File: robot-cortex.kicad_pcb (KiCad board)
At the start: 2 copper layers, 11 parts, among them U3 DF52-5S-0.8H(21)

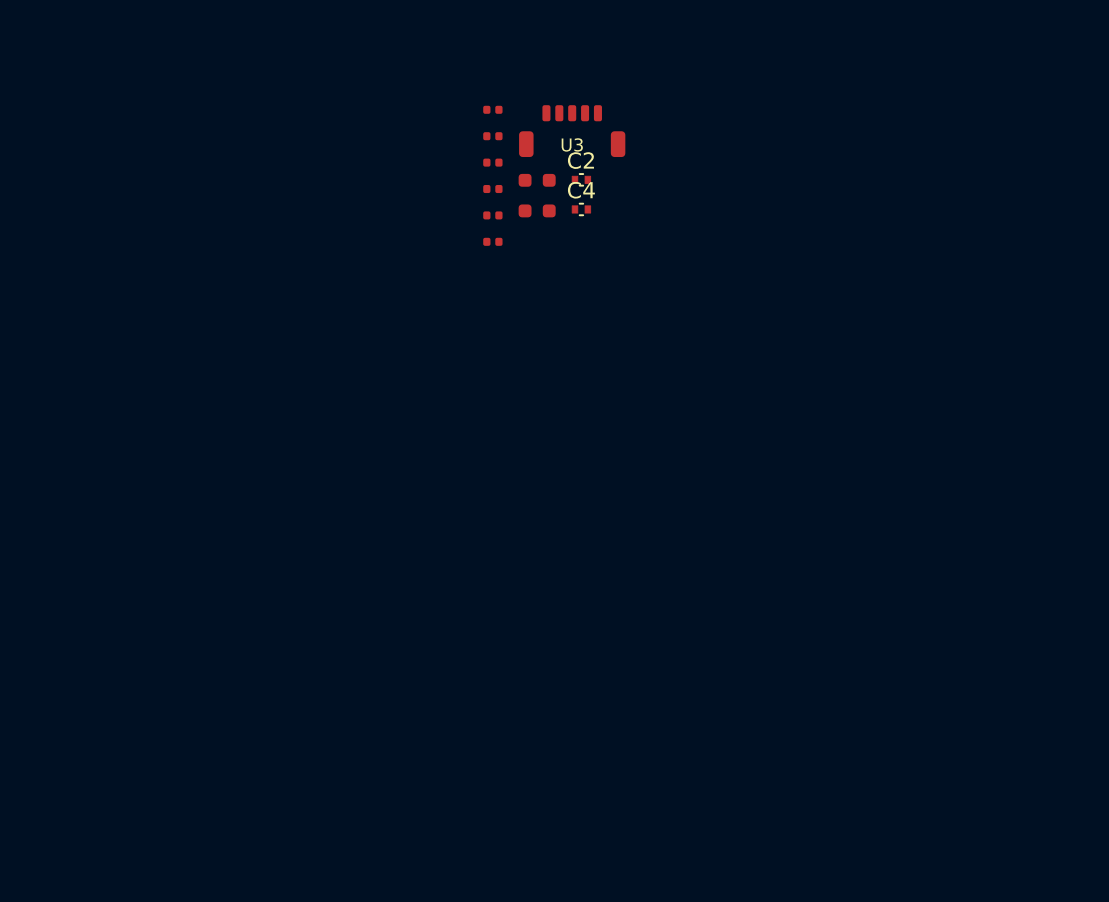
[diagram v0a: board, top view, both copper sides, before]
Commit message: added many components
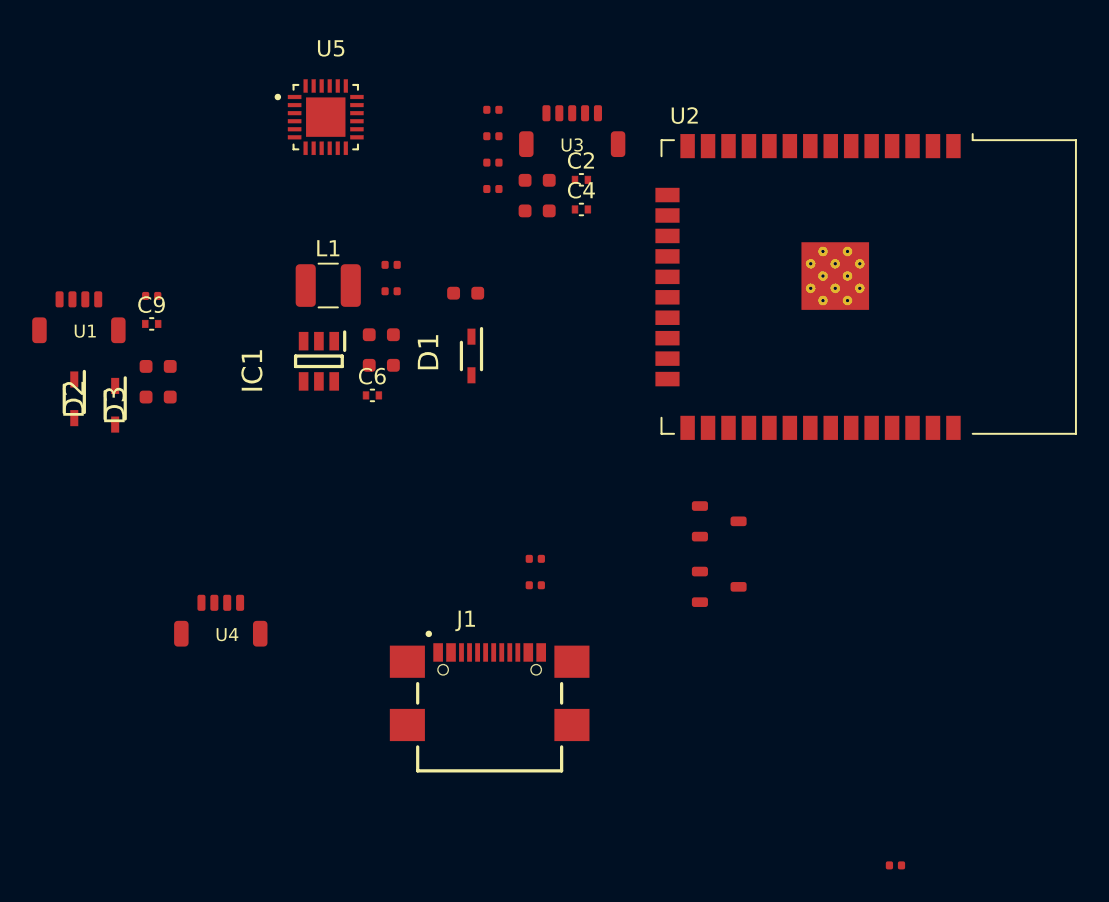
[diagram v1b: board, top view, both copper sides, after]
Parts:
- added C10: 4.7uF, robot-cortex:C_0603_1608Metric, F.Cu at (54.5, 58.2)
- added C11: 4.7uF, robot-cortex:C_0603_1608Metric, F.Cu at (54.5, 60.1)
- added C5: 4.7uF, robot-cortex:C_0603_1608Metric, F.Cu at (73.6, 53.6)
- added C6: 100nF, robot-cortex:C_0402_1005Metric, F.Cu at (67.8, 60.0)
- added C7: 4.7uF, robot-cortex:C_0603_1608Metric, F.Cu at (68.4, 56.2)
- added C8: 4.7uF, robot-cortex:C_0603_1608Metric, F.Cu at (68.4, 58.1)
- added C9: 100nF, robot-cortex:C_0402_1005Metric, F.Cu at (54.1, 55.5)
- added D1: NSR0530HT1G, robot-cortex:SOD2512X110N, F.Cu at (74.0, 57.5)
- added D2: NSR0530HT1G, robot-cortex:SOD2512X110N, F.Cu at (49.3, 60.2)
- added D3: NSR0530HT1G, robot-cortex:SOD2512X110N, F.Cu at (51.9, 60.6)
- added IC1: ADP2301AUJZ-R7, robot-cortex:SOT95P280X100-6N, F.Cu at (64.5, 57.8)
- added J1: USB4110GFA, robot-cortex:GCT_USB4110GFA, F.Cu at (75.1, 77.0)
- added L1: 2.2uH, Inductor_SMD:L_1210_3225Metric, F.Cu at (65.1, 53.1)
- added Q1: NPN, robot-cortex:SOT-23-3, F.Cu at (89.4, 67.8)
- added Q2: NPN, robot-cortex:SOT-23-3, F.Cu at (89.4, 71.8)
- added R11: 10.2k, robot-cortex:R_0402_1005Metric, F.Cu at (69.0, 53.5)
- added R7: 5.1k, robot-cortex:R_0402_1005Metric, F.Cu at (77.9, 70.1)
- added R8: 5.1k, robot-cortex:R_0402_1005Metric, F.Cu at (77.9, 71.8)
- added R9: 1k, robot-cortex:R_0402_1005Metric, F.Cu at (100.3, 89.2)
- added U1: DF52-4S-0.8H(21), robot-cortex:DF52-4S-0.8H(21), F.Cu at (49.6, 54.0)
- added U2: ESP32-WROOM-32E-H4, robot-cortex:ESP32-WROOM-32, F.Cu at (95.7, 53.2)
- added U4: DF52-4S-0.8H(21), robot-cortex:DF52-4S-0.8H(21), F.Cu at (58.4, 72.8)
- added U5: CP2102N-A02-GQFN24R, robot-cortex:QFN50P400X400X80-25N, F.Cu at (64.9, 42.7)
- R5: value 10k -> 31.6k
- R6: value 2k -> 10k
- moved R6 21.5 mm to (54.1, 53.8)
- moved R5 7.03 mm to (69.0, 51.9)
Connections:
- C1 pad 1: /3V3 -> 3v3
- C2 pad 1: /3V3 -> 3v3
- C3 pad 1: /3V3 -> 3v3
- C4 pad 1: /3V3 -> 3v3
- R5 pad 1: Net-(U1-SUSPENDb) -> /3V3-Supply/FB
- R5 pad 2: GND -> 3v3
- R6 pad 1: Net-(U1-RSTb) -> /EN
- R6 pad 2: /3V3 -> 3v3

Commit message: checked and fixed npn issue, added mpn
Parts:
- Q1, Q2: value NPN -> SS8050-G
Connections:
- Q1 pad 2: /EN -> /RTS
- Q1 pad 3: /RTS -> /EN
- Q2 pad 2: /IO0 -> /DTR
- Q2 pad 3: /DTR -> /IO0
- U5 pad 10: (no net) -> unconnected-(U5-NC-Pad10)
- U5 pad 16: (no net) -> unconnected-(U5-NC-Pad16)
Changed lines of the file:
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@@
   (net 63 "unconnected-(U5-~{CTS}-Pad18)")
   (net 64 "/VBAT")
+  (net 65 "unconnected-(U5-NC-Pad10)")
+  (net 66 "unconnected-(U5-NC-Pad16)")
   (footprint "robot-cortex:R_0402_1005Metric" (layer "F.Cu")
     (at 77.945 70.11)
@@
       (net 9 "Net-(U5-~{RST})") (pinfunction "~{RST}") (pintype "bidirectional") (solder_mask_margin 0.102))
     (pad "10" smd roundrect (at 0.25 1.935 90) (size 0.84 0.26) (layers "F.Cu" "F.Paste" "F.Mask") (roundrect_rratio 0.03)
-      (solder_mask_margin 0.102))
+      (net 65 "unconnected-(U5-NC-Pad10)") (pinfunction "NC") (pintype "no_connect") (solder_mask_margin 0.102))
     (pad "11" smd roundrect (at 0.75 1.935 90) (size 0.84 0.26) (layers "F.Cu" "F.Paste" "F.Mask") (roundrect_rratio 0.03)
       (net 54 "unconnected-(U5-GPIO.3{slash}WAKEUP-Pad11)") (pinfunction "GPIO.3/WAKEUP") (pintype "bidirectional+no_connect") (solder_mask_margin 0.102))
@@
       (net 61 "unconnected-(U5-SUSPENDB-Pad15)") (pinfunction "SUSPENDB") (pintype "output+no_connect") (solder_mask_margin 0.102))
     (pad "16" smd roundrect (at 1.935 -0.25) (size 0.84 0.26) (layers "F.Cu" "F.Paste" "F.Mask") (roundrect_rratio 0.03)
-      (solder_mask_margin 0.102))
+      (net 66 "unconnected-(U5-NC-Pad16)") (pinfunction "NC") (pintype "no_connect") (solder_mask_margin 0.102))
     (pad "17" smd roundrect (at 1.935 -0.75) (size 0.84 0.26) (layers "F.Cu" "F.Paste" "F.Mask") (roundrect_rratio 0.03)
       (net 62 "unconnected-(U5-SUSPEND-Pad17)") (pinfunction "SUSPEND") (pintype "output+no_connect") (solder_mask_margin 0.102))
@@
         (effects (font (size 1 1) (thickness 0.15)))
     )
-    (fp_text value "NPN" (at 0 2.4) (layer "F.Fab") hide
+    (fp_text value "SS8050-G" (at 0 2.4) (layer "F.Fab") hide
         (effects (font (size 1 1) (thickness 0.15)))
     )
@@
       (net 6 "Net-(Q2-B)") (pinfunction "B") (pintype "input") (solder_mask_margin 0.0508))
     (pad "2" smd roundrect (at -1.2 0.95) (size 1 0.6) (layers "F.Cu" "F.Paste" "F.Mask") (roundrect_rratio 0.25)
+      (net 3 "/DTR") (pinfunction "E") (pintype "open_emitter") (solder_mask_margin 0.0508))
+    (pad "3" smd roundrect (at 1.2 0) (size 1 0.6) (layers "F.Cu" "F.Paste" "F.Mask") (roundrect_rratio 0.25)
       (net 31 "/IO0") (pinfunction "C") (pintype "open_collector") (solder_mask_margin 0.0508))
-    (pad "3" smd roundrect (at 1.2 0) (size 1 0.6) (layers "F.Cu" "F.Paste" "F.Mask") (roundrect_rratio 0.25)
-      (net 3 "/DTR") (pinfunction "E") (pintype "open_emitter") (solder_mask_margin 0.0508))
     (model "${KIPRJMOD}/3dModels/SOT-23.step"
       (offset (xyz 0 0 0))
@@
         (effects (font (size 1 1) (thickness 0.15)))
     )
-    (fp_text value "NPN" (at 0 2.4) (layer "F.Fab") hide
+    (fp_text value "SS8050-G" (at 0 2.4) (layer "F.Fab") hide
         (effects (font (size 1 1) (thickness 0.15)))
     )
@@
       (net 4 "Net-(Q1-B)") (pinfunction "B") (pintype "input") (solder_mask_margin 0.0508))
     (pad "2" smd roundrect (at -1.2 0.95) (size 1 0.6) (layers "F.Cu" "F.Paste" "F.Mask") (roundrect_rratio 0.25)
+      (net 5 "/RTS") (pinfunction "E") (pintype "open_emitter") (solder_mask_margin 0.0508))
+    (pad "3" smd roundrect (at 1.2 0) (size 1 0.6) (layers "F.Cu" "F.Paste" "F.Mask") (roundrect_rratio 0.25)
       (net 14 "/EN") (pinfunction "C") (pintype "open_collector") (solder_mask_margin 0.0508))
-    (pad "3" smd roundrect (at 1.2 0) (size 1 0.6) (layers "F.Cu" "F.Paste" "F.Mask") (roundrect_rratio 0.25)
-      (net 5 "/RTS") (pinfunction "E") (pintype "open_emitter") (solder_mask_margin 0.0508))
     (model "${KIPRJMOD}/3dModels/SOT-23.step"
       (offset (xyz 0 0 0))

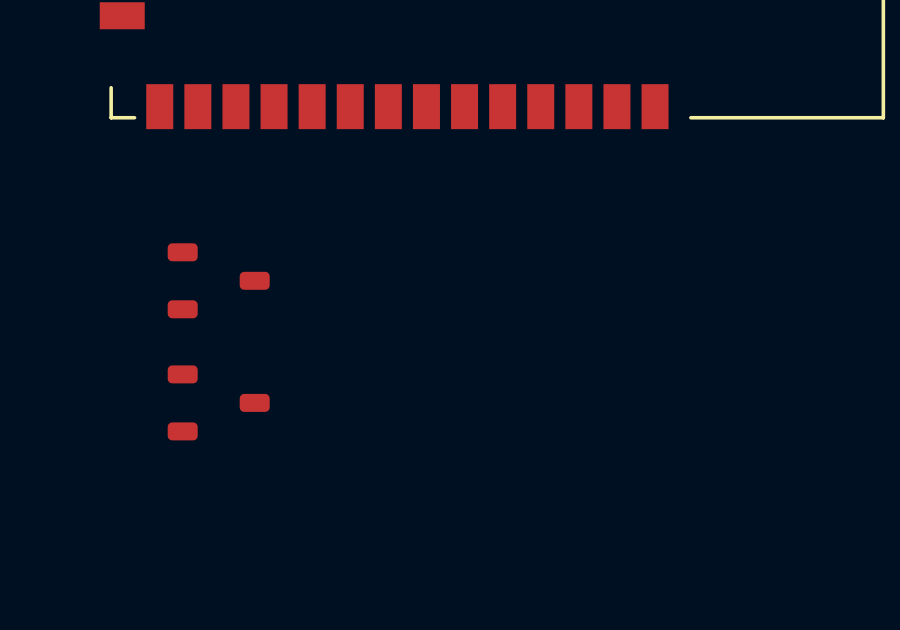
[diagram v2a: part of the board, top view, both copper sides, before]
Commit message: added tvs diodes, schematic review. Probably gonna axe the external uart for this one
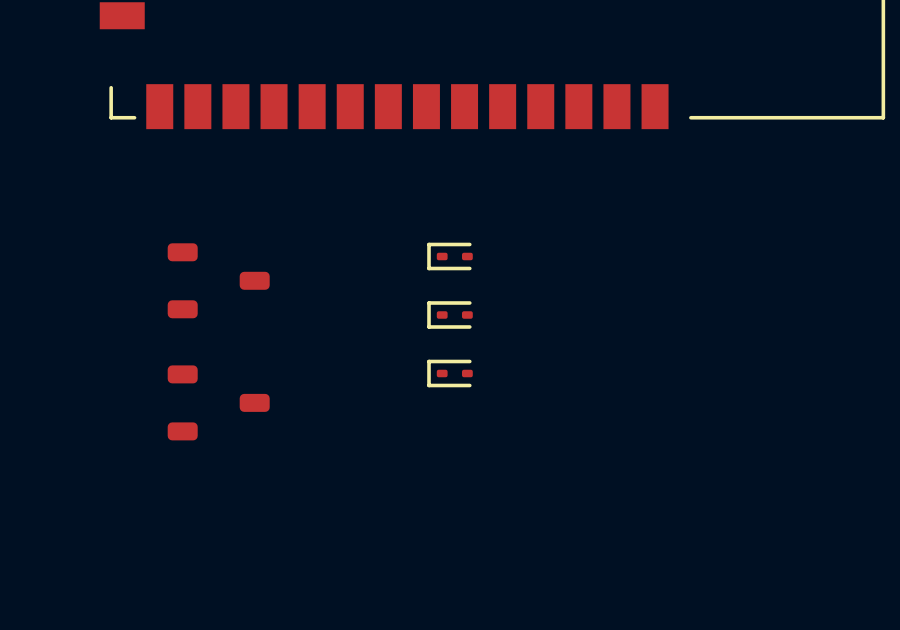
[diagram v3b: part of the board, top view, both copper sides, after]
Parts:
- added D4: ESD9B3.3ST5G, robot-cortex:D_SOD-923, F.Cu at (97.2, 67.0)
- added D5: ESD9B3.3ST5G, robot-cortex:D_SOD-923, F.Cu at (97.2, 68.9)
- added D6: ESD9B3.3ST5G, robot-cortex:D_SOD-923, F.Cu at (97.2, 70.9)
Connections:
- U2 pad 29: unconnected-(U2-IO5-Pad29) -> /ESP32_SS
- U2 pad 30: unconnected-(U2-IO18-Pad30) -> /ESP32_SCK
- U2 pad 31: unconnected-(U2-IO19-Pad31) -> /ESP32_MISO
- U2 pad 37: unconnected-(U2-IO23-Pad37) -> /ESP32_MOSI

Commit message: moved esp32 to heirarchichalca
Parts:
- R3: value 22k -> 1k
- R4: value 47.5k -> 22k
- R9: value 1k -> 47.5k
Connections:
- net /CP210x_RX renamed /ESP32/CP210x_RX
- net /CP210x_TX renamed /ESP32/CP210x_TX
- net /EN renamed /ESP32/EN
- net /ESP32_MISO renamed /ESP32/ESP32_MISO
- net /ESP32_MOSI renamed /ESP32/ESP32_MOSI
- net /ESP32_SCK renamed /ESP32/ESP32_SCK
- net /ESP32_SS renamed /ESP32/ESP32_SS
- net /ESP_UART2_RX renamed /ESP32/ESP_UART2_RX
- net /ESP_UART2_TX renamed /ESP32/ESP_UART2_TX
- net /IO0 renamed /ESP32/IO0
- net /TCK renamed /ESP32/TCK
- net /TDI renamed /ESP32/TDI
- net /TDO renamed /ESP32/TDO
- net /TMS renamed /ESP32/TMS
- Q1 pad 2: /RTS -> /ESP32/RTS
- Q2 pad 2: /DTR -> /ESP32/DTR
- R1 pad 1: /DTR -> /ESP32/RTS
- R1 pad 2: Net-(Q1-B) -> Net-(Q2-B)
- R2 pad 1: /RTS -> /ESP32/DTR
- R2 pad 2: Net-(Q2-B) -> Net-(Q1-B)
- R3 pad 1: /CP210x_VBUS -> Net-(U5-~{RST})
- R3 pad 2: /VUSB -> 3v3
- R4 pad 1: GND -> /ESP32/CP210x_VBUS
- R4 pad 2: /CP210x_VBUS -> /ESP32/VUSB
- R9 pad 1: Net-(U5-~{RST}) -> GND
- R9 pad 2: 3v3 -> /ESP32/CP210x_VBUS
- U5 pad 19: /RTS -> /ESP32/RTS
- U5 pad 23: /DTR -> /ESP32/DTR
- U5 pad 8: /CP210x_VBUS -> /ESP32/CP210x_VBUS

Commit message: commit b4 transition to non-coprocessor. most of sch is done which is good
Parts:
- removed U4: DF52-4S-0.8H(21), robot-cortex:DF52-4S-0.8H(21)
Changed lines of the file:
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@@
-    )
-  )
-  (footprint "robot-cortex:DF52-4S-0.8H(21)" (layer "F.Cu")
-    (at 58.41 72.84)
-    (property "Field2" "")
-    (property "Sheetfile" "ESP32.kicad_sch")
-    (property "Sheetname" "ESP32")
-    (attr smd)
-    (fp_text reference "U4" (at 0.4 2 unlocked) (layer "F.SilkS")
-        (effects (font (size 0.8 0.8) (thickness 0.15)))
-    )
-    (fp_text value "DF52-4S-0.8H(21)" (at 0 1 unlocked) (layer "F.Fab") hide
-        (effects (font (size 1 1) (thickness 0.15)))
-    )
-    (fp_text user "${REFERENCE}" (at 0.4 2 unlocked) (layer "F.Fab")
-        (effects (font (size 0.3 0.3) (thickness 0.075)))
-    )
-    (fp_rect (start -2.902 -0.508) (end 2.902 2.694)
-      (stroke (width 0.05) (type default)) (fill none) (layer "F.CrtYd"))
-    (pad "1" smd roundrect (at -1.2 0 180) (size 0.5 1) (layers "F.Cu" "F.Paste" "F.Mask") (roundrect_rratio 0.25)
-      (net 1 "3v3") (pinfunction "1") (pintype "input") (thermal_bridge_angle 45))
-    (pad "2" smd roundrect (at -0.4 0 180) (size 0.5 1) (layers "F.Cu" "F.Paste" "F.Mask") (roundrect_rratio 0.25)
-      (net 34 "/ESP32/ESP_UART2_RX") (pinfunction "2") (pintype "input") (thermal_bridge_angle 45))
-    (pad "3" smd roundrect (at 0.4 0 180) (size 0.5 1) (layers "F.Cu" "F.Paste" "F.Mask") (roundrect_rratio 0.25)
-      (net 35 "/ESP32/ESP_UART2_TX") (pinfunction "3") (pintype "input") (thermal_bridge_angle 45))
-    (pad "4" smd roundrect (at 1.2 0 180) (size 0.5 1) (layers "F.Cu" "F.Paste" "F.Mask") (roundrect_rratio 0.25)
-      (net 2 "GND") (pinfunction "4") (pintype "input") (thermal_bridge_angle 45))
-    (pad "5" smd roundrect (at 2.45 1.92) (size 0.9 1.6) (layers "F.Cu" "F.Paste" "F.Mask") (roundrect_rratio 0.25)
-      (net 2 "GND") (pinfunction "MNT") (pintype "input") (solder_mask_margin 0.0508) (thermal_bridge_angle 45))
-    (pad "6" smd roundrect (at -2.45 1.92) (size 0.9 1.6) (layers "F.Cu" "F.Paste" "F.Mask") (roundrect_rratio 0.25)
-      (net 2 "GND") (pinfunction "MNT") (pintype "input") (solder_mask_margin 0.0508) (thermal_bridge_angle 45))
-    (model "${KIPRJMOD}/3dModels/DF52-4S-0.8H.stp"
-      (offset (xyz -20.1 1 -3.9))
-      (scale (xyz 1 1 1))
-      (rotate (xyz 0 0 0))
     )
   )

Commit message: heirarchichal sheet label error fix
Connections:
- R4 pad 2: /ESP32/VUSB -> /VUSB
